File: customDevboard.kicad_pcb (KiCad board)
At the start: 4 copper layers, 40 x 40 mm, 87 parts, among them J1 Conn_01x01, J10 Conn_01x01, J11 Conn_01x01, J12 Conn_01x01, J13 Conn_01x01, J14 Conn_01x01, J15 Conn_01x01, J16 Conn_01x01, J17 Conn_01x01, J18 Conn_01x01, J19 Conn_01x01, J2 USB_C_Receptacle_USB2.0_14P, J20 From BEC, J21 Conn_01x01, J22 Conn_01x01, J23 Conn_01x01, J24 Conn_01x01, J25 Conn_01x01, J26 Conn_01x01, J27 Conn_01x01, J3 Conn_01x01, J4 Conn_01x01, J5 Conn_01x01, J6 Debug, J7 To GPS, J8 BZ+, J9 COL, Q1 BC817, Q2 AO3401A, U1 DPS310, U3 TPD2EUSB30, U5 STM32F722RET6, U6 TLV75733PDRV, U7 BMI270, Y1 8MHz, Y2 32.768KHz

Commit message: firmware and readme
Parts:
- added J28: PA6, Connector_Wire:SolderWirePad_1x01_SMD_1x2mm, F.Cu at (27.0, 50.2)
- added J29: PA5, Connector_Wire:SolderWirePad_1x01_SMD_1x2mm, F.Cu at (28.5, 50.2)
- added J30: PC1, Connector_Wire:SolderWirePad_1x01_SMD_1x2mm, F.Cu at (25.5, 53.5)
- added J31: PC11, Connector_Wire:SolderWirePad_1x01_SMD_1x2mm, F.Cu at (27.0, 53.5)
- added J32: PB13, Connector_Wire:SolderWirePad_1x01_SMD_1x2mm, F.Cu at (28.5, 53.5)
- added J33: PA4, Connector_Wire:SolderWirePad_1x01_SMD_1x2mm, F.Cu at (20.5, 29.8)
- added J34: PB2, Connector_Wire:SolderWirePad_1x01_SMD_1x2mm, F.Cu at (20.5, 28.2)
- added J35: PC11, Connector_Wire:SolderWirePad_1x01_SMD_1x2mm, F.Cu at (20.5, 26.8)
- added J36: PC10, Connector_Wire:SolderWirePad_1x01_SMD_1x2mm, F.Cu at (20.5, 25.2)
- added J37: PB6, Connector_Wire:SolderWirePad_1x01_SMD_1x2mm, F.Cu at (17.5, 26.2)
- added J38: PB7, Connector_Wire:SolderWirePad_1x01_SMD_1x2mm, F.Cu at (17.5, 24.8)
- added J39: PA9, Connector_Wire:SolderWirePad_1x01_SMD_1x2mm, F.Cu at (17.5, 29.8)
- added J40: PA10, Connector_Wire:SolderWirePad_1x01_SMD_1x2mm, F.Cu at (17.5, 28.2)
- added J41: PA2, Connector_Wire:SolderWirePad_1x01_SMD_1x2mm, F.Cu at (21.0, 31.8)
- added J42: PA3, Connector_Wire:SolderWirePad_1x01_SMD_1x2mm, F.Cu at (21.0, 33.2)
- added J43: PB10, Connector_Wire:SolderWirePad_1x01_SMD_1x2mm, F.Cu at (30.8, 50.5)
- added J44: PB11, Connector_Wire:SolderWirePad_1x01_SMD_1x2mm, F.Cu at (32.2, 50.5)
- J25: value Conn_01x01 -> PA0
- J26: value Conn_01x01 -> PA1
- J27: value Conn_01x01 -> PA7
- moved D1 7.08 mm to (23.8, 30.0), turned to 180 degrees
- moved R19 5.48 mm to (24.2, 28.5), turned to 180 degrees
- moved J27 3.67 mm to (25.5, 50.2)
- moved J14 1.75 mm to (43.0, 53.4)
- moved J15 1.75 mm to (41.5, 53.4)
- moved J16 1.75 mm to (40.0, 53.4)
- moved J17 1.75 mm to (38.5, 53.4)
- moved J18 1.75 mm to (37.0, 53.4)
- moved J19 1.75 mm to (35.5, 53.4)
- moved J21 1.75 mm to (34.0, 53.4)
- moved J22 1.75 mm to (32.5, 53.4)
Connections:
- J27 pad 1: PB2 -> SPI1_MOSI
- U5 pad 27: PB2 -> SPI3_MOSI
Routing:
- net SPI2_MOSI: track 0.00 -> 31.0 mm, vias 0 -> 2
- net USART3_RX: track 0.00 -> 28.8 mm, vias 0 -> 2
- net SPI3_MOSI: track 0.00 -> 27.7 mm, vias 0 -> 2
- net SPI2_MISO: track 0.00 -> 27.4 mm, vias 0 -> 2
- net SPI2_SCK: track 0.00 -> 26.2 mm, vias 0 -> 2
- net SPI1_MOSI: track 5.01 -> 30.5 mm, vias 0 -> 2
- net SPI3_SCK: track 0.00 -> 23.4 mm, vias 0 -> 2
- net USART1_RX: track 24.9 -> 47.6 mm, vias 1 -> 2
- net USART1_TX: track 23.4 -> 45.6 mm, vias 1 -> 5
- net SPI3_MISO: track 0.00 -> 21.6 mm, vias 0 -> 2
- net I2C1_SCL: track 35.1 -> 55.6 mm, vias 2 -> 4
- net PB2: track 20.1 -> 0.00 mm
- net SPI3_NSS: track 0.00 -> 20.0 mm, vias 0 -> 2
- net SPI1_MISO: track 4.21 -> 24.1 mm, vias 0 -> 2
- net USART2_RX: track 0.00 -> 19.7 mm, vias 0 -> 2
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
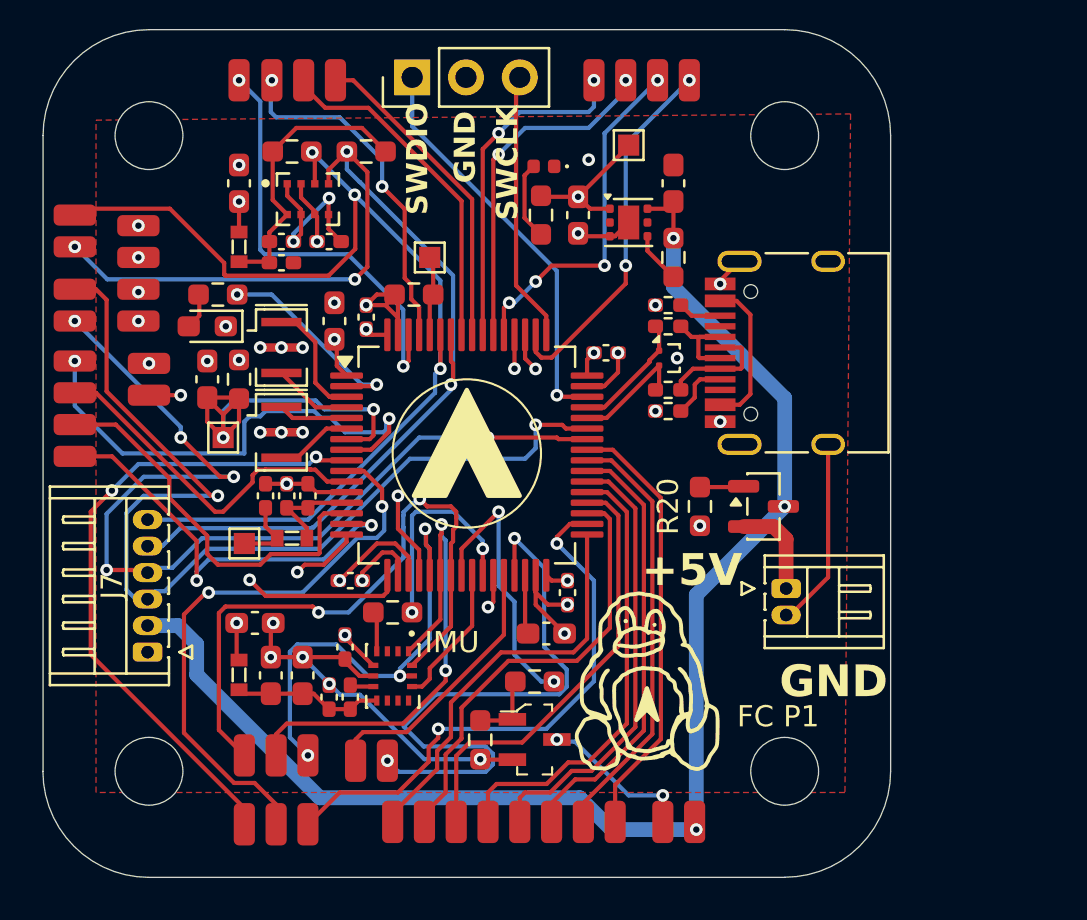
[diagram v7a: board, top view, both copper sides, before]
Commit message: add switches and fix drc
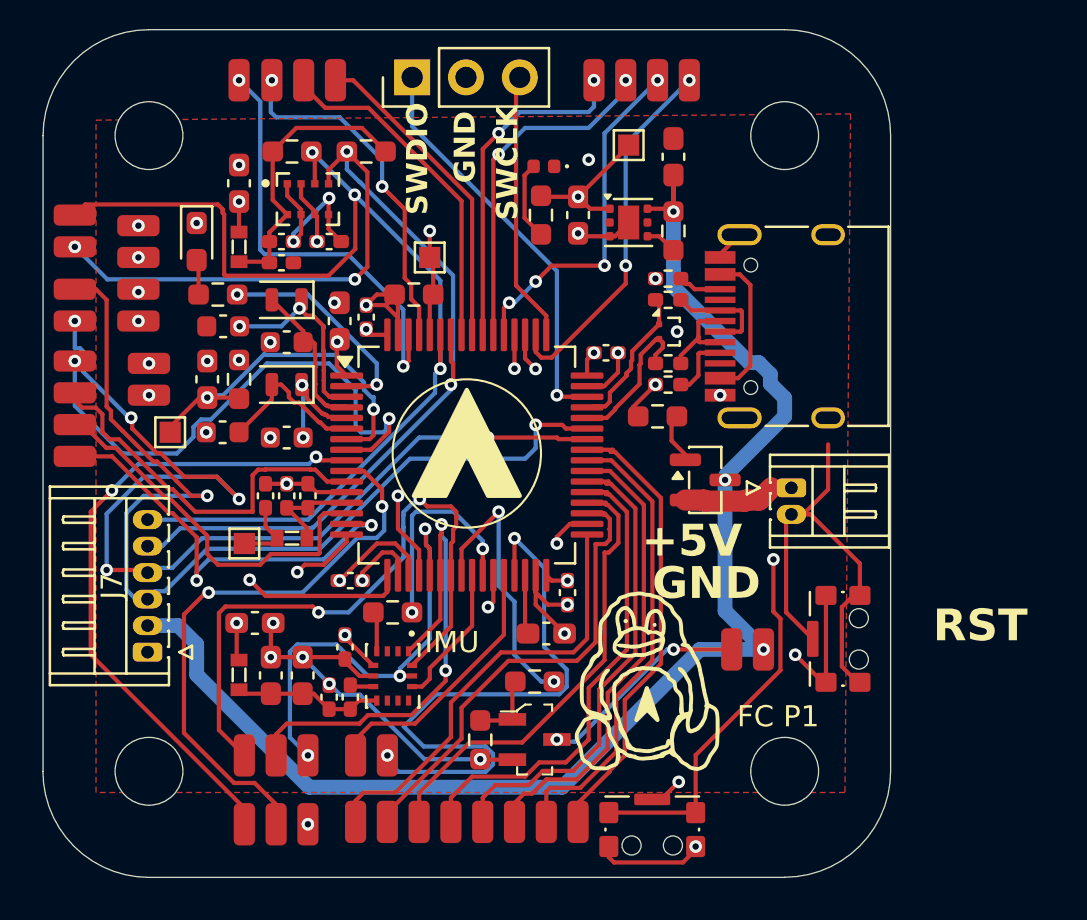
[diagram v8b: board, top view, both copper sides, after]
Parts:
- added C11: 8pF, Capacitor_SMD:C_0603_1608Metric, F.Cu at (24.5, 35.0)
- added C12: 12.5pF, Capacitor_SMD:C_0603_1608Metric, F.Cu at (24.5, 30.0)
- added C13: 12.5pF, Capacitor_SMD:C_0603_1608Metric, F.Cu at (27.5, 30.8)
- added C9: 8pF, Capacitor_SMD:C_0603_1608Metric, F.Cu at (27.5, 35.2)
- added SW1: CK_KMS2xxGP, Button_Switch_SMD:SW_SPST_CK_KMS2xxGP, F.Cu at (53.8, 44.8)
- added SW2: CK_KMS2xxGP, Button_Switch_SMD:SW_SPST_CK_KMS2xxGP, F.Cu at (44.8, 53.8)
- Y1: value 8MHz -> 32.768KHz; footprint Crystal:Resonator_SMD_Murata_CSTxExxV-3Pin_3.0x1.1mm -> Crystal:Crystal_SMD_2012-2Pin_2.0x1.2mm
- Y2: value 32.768KHz -> 8Mhz; footprint Crystal:Resonator_SMD_Murata_CSTxExxV-3Pin_3.0x1.1mm -> Crystal:Crystal_SMD_2012-2Pin_2.0x1.2mm
- moved J8 8.76 mm to (50.0, 45.2)
- moved J9 8.76 mm to (48.5, 45.2)
- moved Y1 6.25 mm to (27.5, 28.8), turned to 180 degrees
- moved J20 4.76 mm to (51.3, 37.6)
- moved R20 4.70 mm to (45.0, 34.2), turned to 180 degrees
- moved D1 4.03 mm to (23.2, 26.0), turned to -90 degrees
- moved Q2 3.02 mm to (47.2, 37.2)
- moved TP4 2.51 mm to (22.0, 35.0)
- moved Y2 1.77 mm to (27.5, 32.8), turned to 180 degrees
- moved J14 1.75 mm to (41.2, 53.4)
- moved J15 1.75 mm to (39.8, 53.4)
- moved J16 1.75 mm to (38.2, 53.4)
- moved J17 1.75 mm to (36.8, 53.4)
- moved J18 1.75 mm to (35.2, 53.4)
- moved J19 1.75 mm to (33.8, 53.4)
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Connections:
- net Net-(U5-BOOT0) renamed BOOT0
- net Net-(U5-NRST) renamed NRST
- Y1 pad 1: Net-(U5-PH0) -> Net-(U5-PC14)
- Y1 pad 2: GND -> Net-(U5-PC15)
- Y2 pad 1: Net-(U5-PC14) -> Net-(U5-PH0)
- Y2 pad 2: GND -> Net-(U5-PH1)
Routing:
- net BOOT0: track 3.78 -> 45.8 mm, vias 0 -> 2
- net NRST: track 20.4 -> 48.4 mm, vias 2 -> 3
- net GND: track 63.9 -> 79.8 mm, vias 31 -> 27
- net +3.3V: track 43.9 -> 53.8 mm, vias 11 -> 12
- net SPI2_SCK: track 26.2 -> 21.5 mm
- net Net-(U5-PH1): track 3.64 -> 7.41 mm
- net Net-(U5-PC14): track 5.65 -> 9.39 mm, vias 0 -> 2
- net Net-(U5-PC15): track 3.75 -> 7.05 mm
- net USART1_TX: track 45.6 -> 48.4 mm
- net Net-(J9-Pin_1): track 7.70 -> 10.1 mm
- net Net-(U5-PH0): track 3.29 -> 5.50 mm, vias 0 -> 2
- net PC0: track 23.3 -> 25.5 mm
- net I2C1_SDA: track 51.3 -> 52.9 mm
- net PC9: track 20.4 -> 21.9 mm
- net PB12: track 19.4 -> 20.9 mm
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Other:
- board text added: "RST"
